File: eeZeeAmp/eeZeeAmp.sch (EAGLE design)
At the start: 11 parts, among them IC1 LM386

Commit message: Minor updates, added gerbers, zip
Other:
- note added: "GAIN"
- moved on the sheet: C3, R1
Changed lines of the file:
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@@
 <text x="159.258" y="24.13" size="3.81" layer="94">eeZeeAmp</text>
 <text x="231.14" y="24.13" size="3.81" layer="94">R0.1</text>
+<text x="142.24" y="129.54" size="1.778" layer="97">GAIN</text>
 </plain>
 <instances>
@@
 <instance part="C1" gate="G$1" x="162.56" y="111.76" rot="R90"/>
 <instance part="C2" gate="G$1" x="88.9" y="114.3" rot="R90"/>
-<instance part="C3" gate="G$1" x="154.94" y="106.68"/>
-<instance part="R1" gate="G$1" x="154.94" y="91.44" rot="R90"/>
+<instance part="C3" gate="G$1" x="154.94" y="101.6"/>
+<instance part="R1" gate="G$1" x="154.94" y="88.9" rot="R90"/>
 <instance part="R2" gate="1" x="111.76" y="101.6"/>
 <instance part="JP2" gate="A" x="185.42" y="109.22"/>
@@
 <pinref part="C3" gate="G$1" pin="1"/>
 <wire x1="160.02" y1="111.76" x2="154.94" y2="111.76" width="0.1524" layer="91"/>
-<wire x1="154.94" y1="111.76" x2="154.94" y2="109.22" width="0.1524" layer="91"/>
+<wire x1="154.94" y1="111.76" x2="154.94" y2="104.14" width="0.1524" layer="91"/>
 <junction x="154.94" y="111.76"/>
 <pinref part="IC1" gate="G$1" pin="OUT"/>
@@
 <pinref part="C3" gate="G$1" pin="2"/>
 <pinref part="R1" gate="G$1" pin="2"/>
-<wire x1="154.94" y1="96.52" x2="154.94" y2="101.6" width="0.1524" layer="91"/>
+<wire x1="154.94" y1="93.98" x2="154.94" y2="96.52" width="0.1524" layer="91"/>
 </segment>
 </net>
@@
 <junction x="78.74" y="106.68"/>
 <pinref part="JP1" gate="A" pin="4"/>
+<label x="58.42" y="106.68" size="1.778" layer="95"/>
 </segment>
 </net>
@@
 <wire x1="132.08" y1="78.74" x2="137.16" y2="78.74" width="0.1524" layer="91"/>
 <wire x1="137.16" y1="78.74" x2="154.94" y2="78.74" width="0.1524" layer="91"/>
-<wire x1="154.94" y1="78.74" x2="154.94" y2="86.36" width="0.1524" layer="91"/>
+<wire x1="154.94" y1="78.74" x2="154.94" y2="83.82" width="0.1524" layer="91"/>
 <wire x1="182.88" y1="109.22" x2="170.18" y2="109.22" width="0.1524" layer="91"/>
 <wire x1="170.18" y1="109.22" x2="170.18" y2="78.74" width="0.1524" layer="91"/>
@@
 <junction x="137.16" y="78.74"/>
 <pinref part="JP1" gate="A" pin="5"/>
+<label x="58.42" y="104.14" size="1.778" layer="95"/>
 </segment>
 </net>
@@
 <pinref part="JP1" gate="A" pin="3"/>
 <wire x1="53.34" y1="109.22" x2="63.5" y2="109.22" width="0.1524" layer="91"/>
-<label x="63.5" y="109.22" size="1.778" layer="95" rot="MR0"/>
+<label x="58.42" y="109.22" size="1.778" layer="95"/>
 </segment>
 </net>
@@
 <pinref part="JP1" gate="A" pin="2"/>
 <wire x1="53.34" y1="111.76" x2="63.5" y2="111.76" width="0.1524" layer="91"/>
-<label x="63.5" y="111.76" size="1.778" layer="95" rot="MR0"/>
+<label x="58.42" y="111.76" size="1.778" layer="95"/>
 </segment>
 </net>

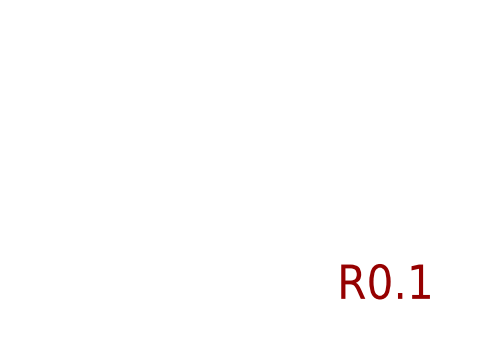
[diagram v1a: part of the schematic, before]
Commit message: Fixed silk pin 1 on LM386, updated version #
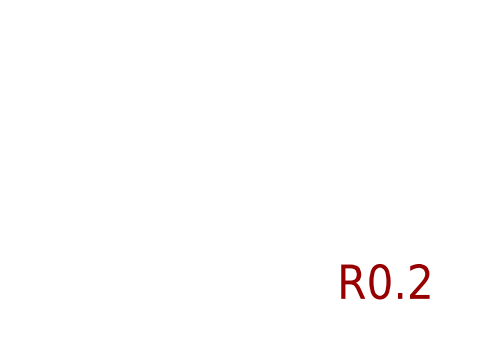
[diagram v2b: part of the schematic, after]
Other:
- note added: "R0.2"
- note removed: "R0.1"
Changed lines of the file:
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@@
 <grid distance="0.1" unitdist="inch" unit="inch" style="lines" multiple="1" display="no" altdistance="0.01" altunitdist="inch" altunit="inch"/>
 <layers>
-<layer number="1" name="Top" color="4" fill="1" visible="yes" active="no"/>
-<layer number="16" name="Bottom" color="1" fill="1" visible="yes" active="no"/>
-<layer number="17" name="Pads" color="2" fill="1" visible="yes" active="no"/>
-<layer number="18" name="Vias" color="2" fill="1" visible="yes" active="no"/>
-<layer number="19" name="Unrouted" color="6" fill="1" visible="yes" active="no"/>
-<layer number="20" name="Dimension" color="15" fill="1" visible="yes" active="no"/>
-<layer number="21" name="tPlace" color="7" fill="1" visible="yes" active="no"/>
-<layer number="22" name="bPlace" color="7" fill="1" visible="yes" active="no"/>
-<layer number="23" name="tOrigins" color="15" fill="1" visible="yes" active="no"/>
-<layer number="24" name="bOrigins" color="15" fill="1" visible="yes" active="no"/>
-<layer number="25" name="tNames" color="7" fill="1" visible="yes" active="no"/>
-<layer number="26" name="bNames" color="7" fill="1" visible="yes" active="no"/>
-<layer number="27" name="tValues" color="7" fill="1" visible="yes" active="no"/>
-<layer number="28" name="bValues" color="7" fill="1" visible="yes" active="no"/>
+<layer number="1" name="Top" color="4" fill="1" visible="no" active="no"/>
+<layer number="16" name="Bottom" color="1" fill="1" visible="no" active="no"/>
+<layer number="17" name="Pads" color="2" fill="1" visible="no" active="no"/>
+<layer number="18" name="Vias" color="2" fill="1" visible="no" active="no"/>
+<layer number="19" name="Unrouted" color="6" fill="1" visible="no" active="no"/>
+<layer number="20" name="Dimension" color="15" fill="1" visible="no" active="no"/>
+<layer number="21" name="tPlace" color="7" fill="1" visible="no" active="no"/>
+<layer number="22" name="bPlace" color="7" fill="1" visible="no" active="no"/>
+<layer number="23" name="tOrigins" color="15" fill="1" visible="no" active="no"/>
+<layer number="24" name="bOrigins" color="15" fill="1" visible="no" active="no"/>
+<layer number="25" name="tNames" color="7" fill="1" visible="no" active="no"/>
+<layer number="26" name="bNames" color="7" fill="1" visible="no" active="no"/>
+<layer number="27" name="tValues" color="7" fill="1" visible="no" active="no"/>
+<layer number="28" name="bValues" color="7" fill="1" visible="no" active="no"/>
 <layer number="29" name="tStop" color="7" fill="3" visible="no" active="no"/>
 <layer number="30" name="bStop" color="7" fill="6" visible="no" active="no"/>
@@
 <layer number="35" name="tGlue" color="7" fill="4" visible="no" active="no"/>
 <layer number="36" name="bGlue" color="7" fill="5" visible="no" active="no"/>
-<layer number="37" name="tTest" color="7" fill="1" visible="yes" active="no"/>
-<layer number="38" name="bTest" color="7" fill="1" visible="yes" active="no"/>
+<layer number="37" name="tTest" color="7" fill="1" visible="no" active="no"/>
+<layer number="38" name="bTest" color="7" fill="1" visible="no" active="no"/>
 <layer number="39" name="tKeepout" color="4" fill="11" visible="no" active="no"/>
 <layer number="40" name="bKeepout" color="1" fill="11" visible="no" active="no"/>
@@
 <layer number="44" name="Drills" color="7" fill="1" visible="no" active="no"/>
 <layer number="45" name="Holes" color="7" fill="1" visible="no" active="no"/>
-<layer number="46" name="Milling" color="3" fill="1" visible="yes" active="no"/>
-<layer number="47" name="Measures" color="7" fill="1" visible="yes" active="no"/>
-<layer number="48" name="Document" color="7" fill="1" visible="yes" active="no"/>
-<layer number="49" name="Reference" color="7" fill="1" visible="yes" active="no"/>
-<layer number="50" name="dxf" color="7" fill="1" visible="yes" active="no"/>
-<layer number="51" name="tDocu" color="7" fill="1" visible="yes" active="no"/>
-<layer number="52" name="bDocu" color="7" fill="1" visible="yes" active="no"/>
-<layer number="53" name="tPadExt" color="7" fill="1" visible="yes" active="no"/>
-<layer number="54" name="bPadExt" color="1" fill="1" visible="yes" active="no"/>
-<layer number="56" name="wert" color="7" fill="1" visible="yes" active="no"/>
+<layer number="46" name="Milling" color="3" fill="1" visible="no" active="no"/>
+<layer number="47" name="Measures" color="7" fill="1" visible="no" active="no"/>
+<layer number="48" name="Document" color="7" fill="1" visible="no" active="no"/>
+<layer number="49" name="Reference" color="7" fill="1" visible="no" active="no"/>
+<layer number="50" name="dxf" color="7" fill="1" visible="no" active="no"/>
+<layer number="51" name="tDocu" color="7" fill="1" visible="no" active="no"/>
+<layer number="52" name="bDocu" color="7" fill="1" visible="no" active="no"/>
+<layer number="53" name="tPadExt" color="7" fill="1" visible="no" active="no"/>
+<layer number="54" name="bPadExt" color="1" fill="1" visible="no" active="no"/>
+<layer number="56" name="wert" color="7" fill="1" visible="no" active="no"/>
 <layer number="90" name="Modules" color="5" fill="1" visible="yes" active="yes"/>
 <layer number="91" name="Nets" color="2" fill="1" visible="yes" active="yes"/>
@@
 <plain>
 <text x="159.258" y="24.13" size="3.81" layer="94">eeZeeAmp</text>
-<text x="231.14" y="24.13" size="3.81" layer="94">R0.1</text>
+<text x="231.14" y="24.13" size="3.81" layer="94">R0.2</text>
 <text x="142.24" y="129.54" size="1.778" layer="97">GAIN</text>
 </plain>

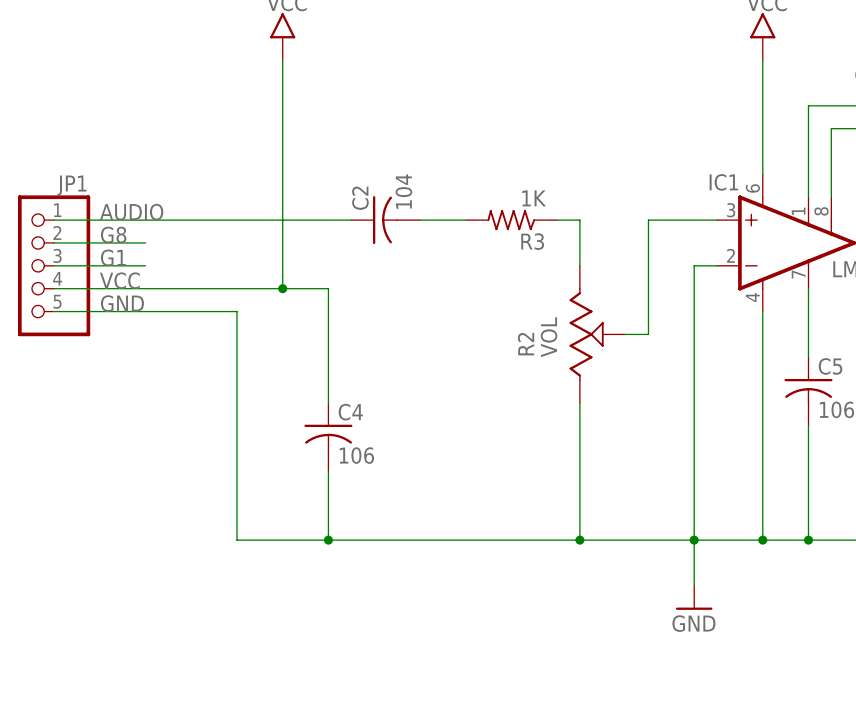
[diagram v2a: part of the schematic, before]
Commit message: Added 0.1uF decoupling cap for LM386 supply
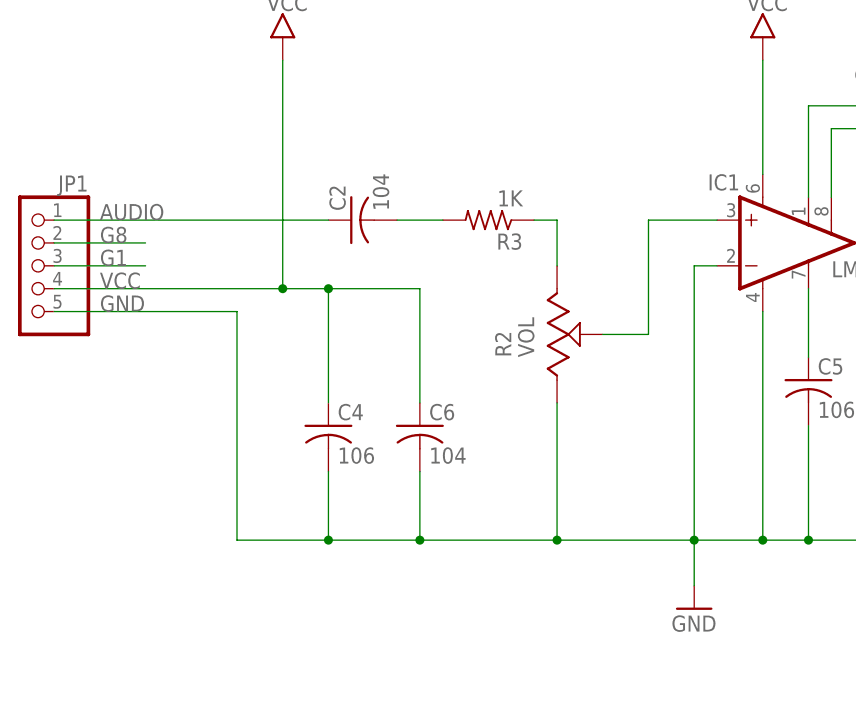
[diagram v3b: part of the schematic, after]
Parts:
- added C6: 104, rcl:C-USC0603
- C1: device rcl:CPOL-USE2.5-6 -> rcl:CPOL-USE3.5-8
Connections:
- net GND: now also C6.2
- net VCC: now also C6.1
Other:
- moved on the sheet: C2, R2, R3
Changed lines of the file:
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@@
 <grid distance="0.1" unitdist="inch" unit="inch" style="lines" multiple="1" display="no" altdistance="0.01" altunitdist="inch" altunit="inch"/>
 <layers>
-<layer number="1" name="Top" color="4" fill="1" visible="no" active="no"/>
-<layer number="16" name="Bottom" color="1" fill="1" visible="no" active="no"/>
-<layer number="17" name="Pads" color="2" fill="1" visible="no" active="no"/>
-<layer number="18" name="Vias" color="2" fill="1" visible="no" active="no"/>
-<layer number="19" name="Unrouted" color="6" fill="1" visible="no" active="no"/>
-<layer number="20" name="Dimension" color="15" fill="1" visible="no" active="no"/>
-<layer number="21" name="tPlace" color="7" fill="1" visible="no" active="no"/>
-<layer number="22" name="bPlace" color="7" fill="1" visible="no" active="no"/>
-<layer number="23" name="tOrigins" color="15" fill="1" visible="no" active="no"/>
-<layer number="24" name="bOrigins" color="15" fill="1" visible="no" active="no"/>
-<layer number="25" name="tNames" color="7" fill="1" visible="no" active="no"/>
-<layer number="26" name="bNames" color="7" fill="1" visible="no" active="no"/>
-<layer number="27" name="tValues" color="7" fill="1" visible="no" active="no"/>
-<layer number="28" name="bValues" color="7" fill="1" visible="no" active="no"/>
+<layer number="1" name="Top" color="4" fill="1" visible="yes" active="no"/>
+<layer number="16" name="Bottom" color="1" fill="1" visible="yes" active="no"/>
+<layer number="17" name="Pads" color="2" fill="1" visible="yes" active="no"/>
+<layer number="18" name="Vias" color="2" fill="1" visible="yes" active="no"/>
+<layer number="19" name="Unrouted" color="6" fill="1" visible="yes" active="no"/>
+<layer number="20" name="Dimension" color="15" fill="1" visible="yes" active="no"/>
+<layer number="21" name="tPlace" color="7" fill="1" visible="yes" active="no"/>
+<layer number="22" name="bPlace" color="7" fill="1" visible="yes" active="no"/>
+<layer number="23" name="tOrigins" color="15" fill="1" visible="yes" active="no"/>
+<layer number="24" name="bOrigins" color="15" fill="1" visible="yes" active="no"/>
+<layer number="25" name="tNames" color="7" fill="1" visible="yes" active="no"/>
+<layer number="26" name="bNames" color="7" fill="1" visible="yes" active="no"/>
+<layer number="27" name="tValues" color="7" fill="1" visible="yes" active="no"/>
+<layer number="28" name="bValues" color="7" fill="1" visible="yes" active="no"/>
 <layer number="29" name="tStop" color="7" fill="3" visible="no" active="no"/>
 <layer number="30" name="bStop" color="7" fill="6" visible="no" active="no"/>
@@
 <layer number="35" name="tGlue" color="7" fill="4" visible="no" active="no"/>
 <layer number="36" name="bGlue" color="7" fill="5" visible="no" active="no"/>
-<layer number="37" name="tTest" color="7" fill="1" visible="no" active="no"/>
-<layer number="38" name="bTest" color="7" fill="1" visible="no" active="no"/>
+<layer number="37" name="tTest" color="7" fill="1" visible="yes" active="no"/>
+<layer number="38" name="bTest" color="7" fill="1" visible="yes" active="no"/>
 <layer number="39" name="tKeepout" color="4" fill="11" visible="no" active="no"/>
 <layer number="40" name="bKeepout" color="1" fill="11" visible="no" active="no"/>
@@
 <layer number="44" name="Drills" color="7" fill="1" visible="no" active="no"/>
 <layer number="45" name="Holes" color="7" fill="1" visible="no" active="no"/>
-<layer number="46" name="Milling" color="3" fill="1" visible="no" active="no"/>
-<layer number="47" name="Measures" color="7" fill="1" visible="no" active="no"/>
-<layer number="48" name="Document" color="7" fill="1" visible="no" active="no"/>
-<layer number="49" name="Reference" color="7" fill="1" visible="no" active="no"/>
-<layer number="50" name="dxf" color="7" fill="1" visible="no" active="no"/>
-<layer number="51" name="tDocu" color="7" fill="1" visible="no" active="no"/>
-<layer number="52" name="bDocu" color="7" fill="1" visible="no" active="no"/>
-<layer number="53" name="tPadExt" color="7" fill="1" visible="no" active="no"/>
-<layer number="54" name="bPadExt" color="1" fill="1" visible="no" active="no"/>
-<layer number="56" name="wert" color="7" fill="1" visible="no" active="no"/>
+<layer number="46" name="Milling" color="3" fill="1" visible="yes" active="no"/>
+<layer number="47" name="Measures" color="7" fill="1" visible="yes" active="no"/>
+<layer number="48" name="Document" color="7" fill="1" visible="yes" active="no"/>
+<layer number="49" name="Reference" color="7" fill="1" visible="yes" active="no"/>
+<layer number="50" name="dxf" color="7" fill="1" visible="yes" active="no"/>
+<layer number="51" name="tDocu" color="7" fill="1" visible="yes" active="no"/>
+<layer number="52" name="bDocu" color="7" fill="1" visible="yes" active="no"/>
+<layer number="53" name="tPadExt" color="7" fill="1" visible="yes" active="no"/>
+<layer number="54" name="bPadExt" color="1" fill="1" visible="yes" active="no"/>
+<layer number="56" name="wert" color="7" fill="1" visible="yes" active="no"/>
 <layer number="90" name="Modules" color="5" fill="1" visible="yes" active="yes"/>
 <layer number="91" name="Nets" color="2" fill="1" visible="yes" active="yes"/>
@@
 <parts>
 <part name="IC1" library="linear" deviceset="LM386?-*" device="M" technology="1" value="LM386"/>
-<part name="C1" library="rcl" deviceset="CPOL-US" device="E2.5-6" value="220uF"/>
+<part name="C1" library="rcl" deviceset="CPOL-US" device="E3.5-8" value="220uF"/>
 <part name="C2" library="rcl" deviceset="C-US" device="C0603" value="104"/>
 <part name="C3" library="rcl" deviceset="C-US" device="C0603" value="503"/>
@@
 <part name="JP1" library="pinhead-2" deviceset="PINHD-1X05" device="_2.54-S"/>
 <part name="FRAME1" library="bt" deviceset="LETTER_L" device=""/>
+<part name="C6" library="rcl" deviceset="C-US" device="C0603" value="104"/>
 </parts>
 <sheets>
@@
 <instance part="IC1" gate="G$1" x="134.62" y="111.76"/>
 <instance part="C1" gate="G$1" x="162.56" y="111.76" rot="R90"/>
-<instance part="C2" gate="G$1" x="88.9" y="114.3" rot="R90"/>
+<instance part="C2" gate="G$1" x="86.36" y="114.3" rot="R90"/>
 <instance part="C3" gate="G$1" x="154.94" y="101.6"/>
 <instance part="R1" gate="G$1" x="154.94" y="88.9" rot="R90"/>
-<instance part="R2" gate="1" x="111.76" y="101.6"/>
+<instance part="R2" gate="1" x="109.22" y="101.6"/>
 <instance part="JP2" gate="A" x="185.42" y="109.22"/>
-<instance part="R3" gate="G$1" x="104.14" y="114.3" rot="R180"/>
+<instance part="R3" gate="G$1" x="101.6" y="114.3" rot="R180"/>
 <instance part="U$1" gate="G$1" x="132.08" y="132.08"/>
 <instance part="U$2" gate="G$1" x="78.74" y="132.08"/>
@@
 <instance part="FRAME1" gate="G$1" x="0" y="0"/>
 <instance part="FRAME1" gate="G$2" x="147.32" y="2.54"/>
+<instance part="C6" gate="G$1" x="93.98" y="91.44"/>
 </instances>
 <busses>
@@
 <wire x1="127" y1="114.3" x2="119.38" y2="114.3" width="0.1524" layer="91"/>
 <wire x1="119.38" y1="114.3" x2="119.38" y2="101.6" width="0.1524" layer="91"/>
-<wire x1="119.38" y1="101.6" x2="116.84" y2="101.6" width="0.1524" layer="91"/>
+<wire x1="119.38" y1="101.6" x2="114.3" y2="101.6" width="0.1524" layer="91"/>
 </segment>
 </net>
@@
 <segment>
 <pinref part="C2" gate="G$1" pin="2"/>
-<wire x1="93.98" y1="114.3" x2="99.06" y2="114.3" width="0.1524" layer="91"/>
+<wire x1="91.44" y1="114.3" x2="96.52" y2="114.3" width="0.1524" layer="91"/>
 <pinref part="R3" gate="G$1" pin="2"/>
 </segment>
@@
 <pinref part="R2" gate="1" pin="E"/>
 <pinref part="R3" gate="G$1" pin="1"/>
-<wire x1="109.22" y1="114.3" x2="111.76" y2="114.3" width="0.1524" layer="91"/>
-<wire x1="111.76" y1="114.3" x2="111.76" y2="109.22" width="0.1524" layer="91"/>
+<wire x1="106.68" y1="114.3" x2="109.22" y2="114.3" width="0.1524" layer="91"/>
+<wire x1="109.22" y1="114.3" x2="109.22" y2="109.22" width="0.1524" layer="91"/>
 </segment>
 </net>
@@
 <pinref part="JP1" gate="A" pin="4"/>
 <label x="58.42" y="106.68" size="1.778" layer="95"/>
+<pinref part="C6" gate="G$1" pin="1"/>
+<wire x1="93.98" y1="93.98" x2="93.98" y2="106.68" width="0.1524" layer="91"/>
+<wire x1="93.98" y1="106.68" x2="83.82" y2="106.68" width="0.1524" layer="91"/>
+<junction x="83.82" y="106.68"/>
 </segment>
 </net>
@@
 <pinref part="C2" gate="G$1" pin="1"/>
 <label x="58.42" y="114.3" size="1.778" layer="95"/>
-<wire x1="53.34" y1="114.3" x2="86.36" y2="114.3" width="0.1524" layer="91"/>
+<wire x1="53.34" y1="114.3" x2="83.82" y2="114.3" width="0.1524" layer="91"/>
 <pinref part="JP1" gate="A" pin="1"/>
 </segment>
@@
 <segment>
 <pinref part="R2" gate="1" pin="A"/>
-<wire x1="111.76" y1="93.98" x2="111.76" y2="78.74" width="0.1524" layer="91"/>
+<wire x1="109.22" y1="93.98" x2="109.22" y2="78.74" width="0.1524" layer="91"/>
 <pinref part="R1" gate="G$1" pin="1"/>
-<wire x1="111.76" y1="78.74" x2="124.46" y2="78.74" width="0.1524" layer="91"/>
+<wire x1="109.22" y1="78.74" x2="124.46" y2="78.74" width="0.1524" layer="91"/>
 <wire x1="124.46" y1="78.74" x2="132.08" y2="78.74" width="0.1524" layer="91"/>
 <wire x1="132.08" y1="78.74" x2="137.16" y2="78.74" width="0.1524" layer="91"/>
@@
 <wire x1="73.66" y1="104.14" x2="73.66" y2="78.74" width="0.1524" layer="91"/>
 <wire x1="73.66" y1="78.74" x2="83.82" y2="78.74" width="0.1524" layer="91"/>
-<junction x="111.76" y="78.74"/>
+<junction x="109.22" y="78.74"/>
 <pinref part="C4" gate="G$1" pin="2"/>
-<wire x1="83.82" y1="78.74" x2="111.76" y2="78.74" width="0.1524" layer="91"/>
+<wire x1="83.82" y1="78.74" x2="93.98" y2="78.74" width="0.1524" layer="91"/>
+<wire x1="93.98" y1="78.74" x2="109.22" y2="78.74" width="0.1524" layer="91"/>
 <wire x1="83.82" y1="86.36" x2="83.82" y2="78.74" width="0.1524" layer="91"/>
 <junction x="83.82" y="78.74"/>
@@
 <pinref part="JP1" gate="A" pin="5"/>
 <label x="58.42" y="104.14" size="1.778" layer="95"/>
-</segment>
-</net>
+<pinref part="C6" gate="G$1" pin="2"/>
+<wire x1="93.98" y1="86.36" x2="93.98" y2="78.74" width="0.1524" layer="91"/>
+<junction x="93.98" y="78.74"/>
+</segment>
+</net>
